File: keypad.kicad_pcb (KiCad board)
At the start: 2 copper layers, 67 x 105 mm, 10 parts, among them SW1 SW_Push, SW2 SW_Push, SW3 SW_Push, SW4 SW_Push, SW5 SW_Push, SW6 SW_Push, SW7 SW_Push, SW8 SW_Push, SW9 SW_Push, U1 ESP32-S3-DevKitC-1

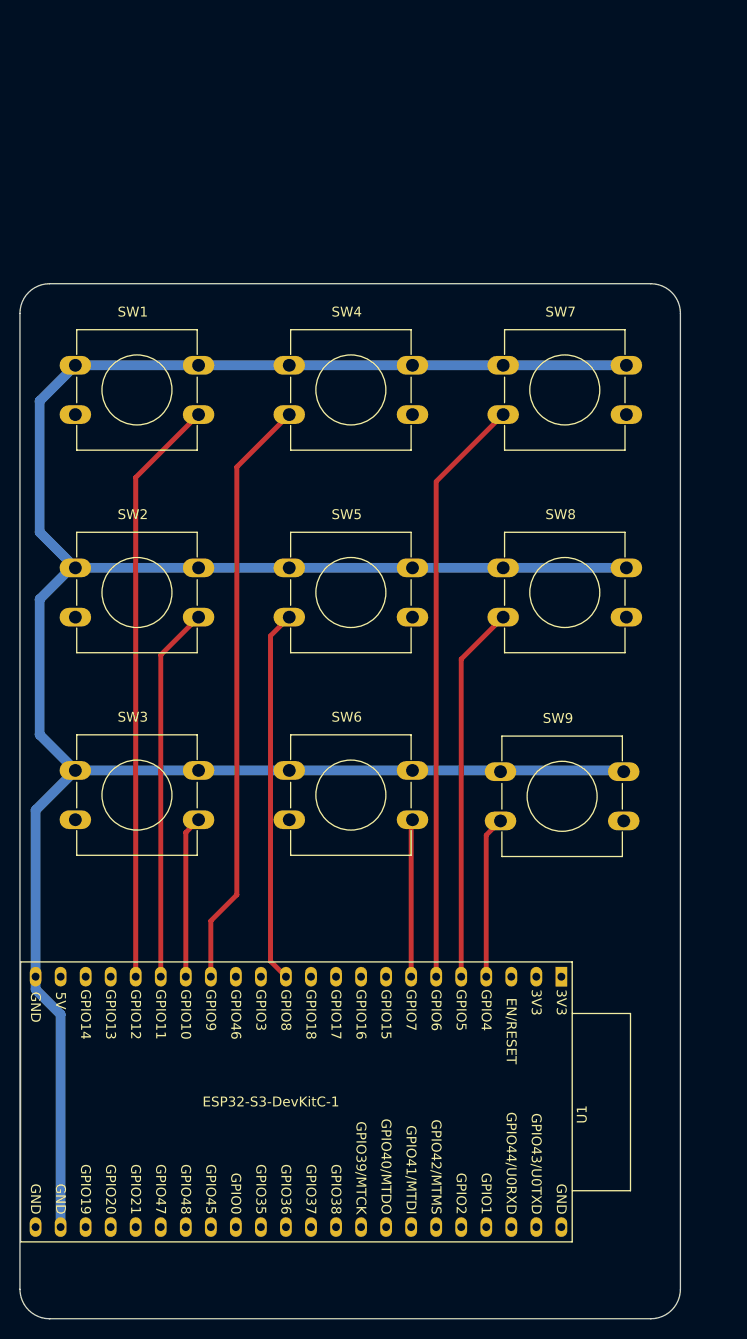
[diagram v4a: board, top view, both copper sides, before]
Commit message: add mounting holes
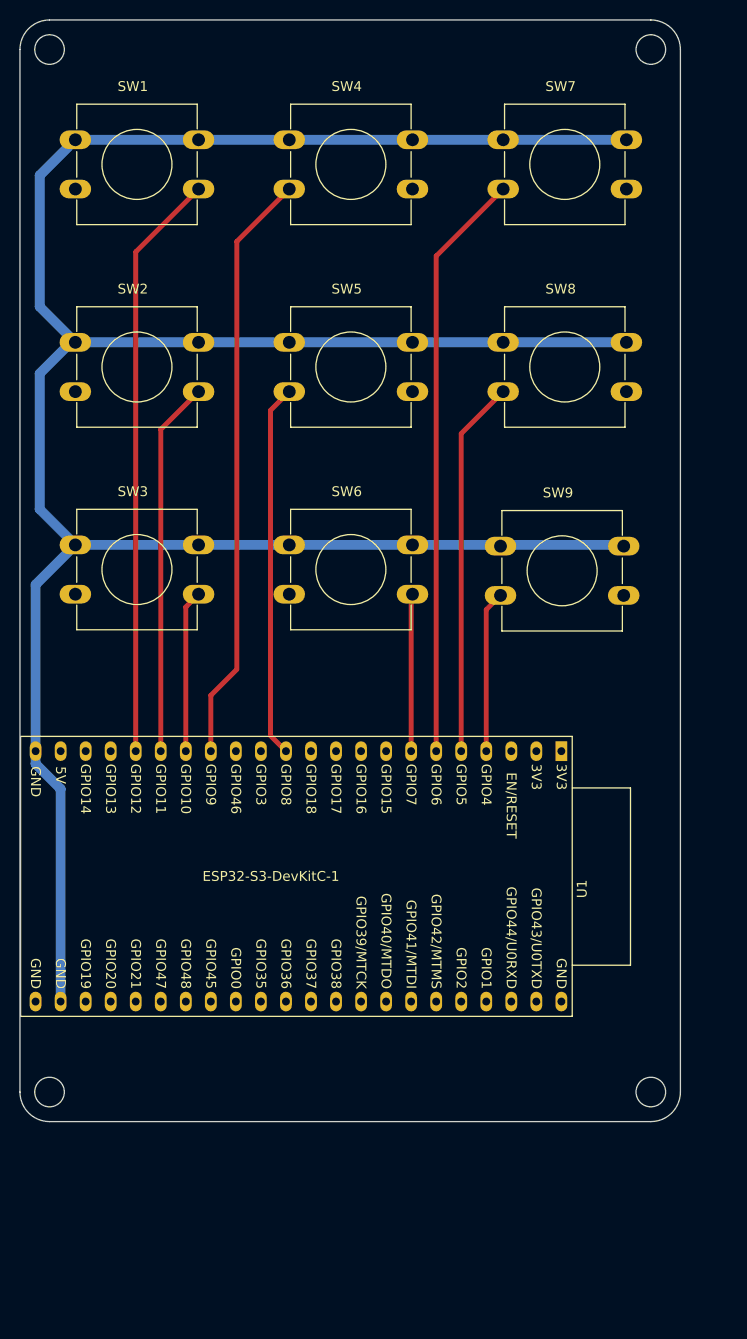
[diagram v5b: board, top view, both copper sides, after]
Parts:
- moved U1 22.9 mm to (172.9, 105.4)
- moved SW1 22.9 mm to (123.6, 43.4)
- moved SW2 22.9 mm to (123.6, 63.9)
- moved SW3 22.9 mm to (123.6, 84.5)
- moved SW4 22.9 mm to (145.3, 43.4)
- moved SW5 22.9 mm to (145.3, 63.9)
- moved SW6 22.9 mm to (145.3, 84.5)
- moved SW7 22.9 mm to (167.0, 43.4)
- moved SW8 22.9 mm to (167.0, 63.9)
- moved SW9 22.9 mm to (166.8, 84.6)
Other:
- board size 67 x 105 mm -> 67 x 111.8 mm

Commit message: add some art
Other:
- board text added: "gavhu10/keypad"
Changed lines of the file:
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@@
 		(capping no)
 		(filling no)
-		(zone_defaults)
 		(pcbplotparams
 			(layerselection 0x00000000_00000000_55555555_5755f5ff)
@@
 	)
 	(gr_line
+		(start 127.015013 96.441276)
+		(end 141.267947 75.971619)
+		(stroke
+			(width 0.839314)
+			(type default)
+		)
+		(layer "B.SilkS")
+	)
+	(gr_line
+		(start 131.082014 96.434741)
+		(end 127.015013 96.441276)
+		(stroke
+			(width 0.839314)
+			(type default)
+		)
+		(layer "B.SilkS")
+	)
+	(gr_line
+		(start 141.267947 75.971619)
+		(end 143.379781 78.326509)
+		(stroke
+			(width 0.839314)
+			(type default)
+		)
+		(layer "B.SilkS")
+	)
+	(gr_line
+		(start 143.379781 78.326509)
+		(end 131.082014 96.434741)
+		(stroke
+			(width 0.839314)
+			(type default)
+		)
+		(layer "B.SilkS")
+	)
+	(gr_line
+		(start 149.633081 85.269967)
+		(end 129.341772 62.68312)
+		(stroke
+			(width 0.839314)
+			(type default)
+		)
+		(layer "B.SilkS")
+	)
+	(gr_line
+		(start 149.636118 62.786378)
+		(end 149.636118 96.531626)
+		(stroke
+			(width 0.839314)
+			(type default)
+		)
+		(layer "B.SilkS")
+	)
+	(gr_line
+		(start 151.57 62.786378)
+		(end 149.636118 62.786378)
+		(stroke
+			(width 0.839314)
+			(type default)
+		)
+		(layer "B.SilkS")
+	)
+	(gr_line
+		(start 151.57 80.88632)
+		(end 151.57 62.786378)
+		(stroke
+			(width 0.839314)
+			(type default)
+		)
+		(layer "B.SilkS")
+	)
+	(gr_line
+		(start 152.614606 46.711926)
+		(end 177.160155 46.711926)
+		(stroke
+			(width 0.839314)
+			(type default)
+		)
+		(layer "B.SilkS")
+	)
+	(gr_line
+		(start 177.160155 46.711926)
+		(end 177.160155 80.88632)
+		(stroke
+			(width 0.839314)
+			(type default)
+		)
+		(layer "B.SilkS")
+	)
+	(gr_line
+		(start 177.160155 80.88632)
+		(end 151.57 80.88632)
+		(stroke
+			(width 0.839314)
+			(type default)
+		)
+		(layer "B.SilkS")
+	)
+	(gr_line
 		(start 118 34.24264)
 		(end 118 140)
@@
 		(layer "Edge.Cuts")
 	)
-	(segment
-		(start 140 53.71632)
-		(end 140 97.12132)
-		(width 0.5)
-		(layer "F.Cu")
-		(net "Net-(U1-GPIO9{slash}ADC1_CH8)")
-	)
-	(segment
-		(start 145.32 48.39632)
-		(end 140 53.71632)
-		(width 0.5)
-		(layer "F.Cu")
-		(net "Net-(U1-GPIO9{slash}ADC1_CH8)")
-	)
-	(segment
-		(start 137.36344 99.75788)
-		(end 137.36344 105.42132)
-		(width 0.5)
-		(layer "F.Cu")
-		(net "Net-(U1-GPIO9{slash}ADC1_CH8)")
-	)
-	(segment
-		(start 140 97.12132)
-		(end 137.36344 99.75788)
-		(width 0.5)
-		(layer "F.Cu")
-		(net "Net-(U1-GPIO9{slash}ADC1_CH8)")
+	(gr_text "gavhu10/keypad"
+		(at 132 138 0)
+		(layer "F.SilkS")
+		(effects
+			(font
+				(size 2 2)
+				(thickness 0.1)
+			)
+			(justify left bottom)
+		)
 	)
 	(segment
@@
 	)
 	(segment
-		(start 134.82344 105.42132)
-		(end 134.82344 90.79288)
+		(start 157.68344 89.63288)
+		(end 157.82 89.49632)
 		(width 0.5)
 		(layer "F.Cu")
-		(net "Net-(U1-GPIO10{slash}ADC1_CH9)")
+		(net "Net-(U1-GPIO7{slash}ADC1_CH6)")
 	)
 	(segment
-		(start 134.82344 90.79288)
-		(end 136.12 89.49632)
+		(start 157.68344 105.42132)
+		(end 157.68344 89.63288)
 		(width 0.5)
 		(layer "F.Cu")
-		(net "Net-(U1-GPIO10{slash}ADC1_CH9)")
+		(net "Net-(U1-GPIO7{slash}ADC1_CH6)")
 	)
 	(segment
-		(start 162.76344 105.42132)
-		(end 162.76344 73.20288)
+		(start 160.22344 105.42132)
+		(end 160.22344 55.19288)
 		(width 0.5)
 		(layer "F.Cu")
-		(net "Net-(U1-GPIO5{slash}ADC1_CH4)")
+		(net "Net-(U1-GPIO6{slash}ADC1_CH5)")
 	)
 	(segment
-		(start 162.76344 73.20288)
-		(end 167.02 68.94632)
+		(start 160.22344 55.19288)
+		(end 167.02 48.39632)
 		(width 0.5)
 		(layer "F.Cu")
-		(net "Net-(U1-GPIO5{slash}ADC1_CH4)")
+		(net "Net-(U1-GPIO6{slash}ADC1_CH5)")
+	)
+	(segment
+		(start 132.28344 105.42132)
+		(end 132.28344 72.78288)
+		(width 0.5)
+		(layer "F.Cu")
+		(net "Net-(U1-GPIO11{slash}ADC2_CH0)")
+	)
+	(segment
+		(start 132.28344 72.78288)
+		(end 136.12 68.94632)
+		(width 0.5)
+		(layer "F.Cu")
+		(net "Net-(U1-GPIO11{slash}ADC2_CH0)")
 	)
 	(segment
@@
 	)
 	(segment
-		(start 160.22344 105.42132)
-		(end 160.22344 55.19288)
+		(start 162.76344 105.42132)
+		(end 162.76344 73.20288)
 		(width 0.5)
 		(layer "F.Cu")
-		(net "Net-(U1-GPIO6{slash}ADC1_CH5)")
+		(net "Net-(U1-GPIO5{slash}ADC1_CH4)")
 	)
 	(segment
-		(start 160.22344 55.19288)
-		(end 167.02 48.39632)
+		(start 162.76344 73.20288)
+		(end 167.02 68.94632)
 		(width 0.5)
 		(layer "F.Cu")
-		(net "Net-(U1-GPIO6{slash}ADC1_CH5)")
+		(net "Net-(U1-GPIO5{slash}ADC1_CH4)")
 	)
 	(segment
-		(start 157.68344 89.63288)
-		(end 157.82 89.49632)
+		(start 140 53.71632)
+		(end 140 97.12132)
 		(width 0.5)
 		(layer "F.Cu")
-		(net "Net-(U1-GPIO7{slash}ADC1_CH6)")
+		(net "Net-(U1-GPIO9{slash}ADC1_CH8)")
 	)
 	(segment
-		(start 157.68344 105.42132)
-		(end 157.68344 89.63288)
+		(start 145.32 48.39632)
+		(end 140 53.71632)
 		(width 0.5)
 		(layer "F.Cu")
-		(net "Net-(U1-GPIO7{slash}ADC1_CH6)")
+		(net "Net-(U1-GPIO9{slash}ADC1_CH8)")
 	)
 	(segment
-		(start 132.28344 105.42132)
-		(end 132.28344 72.78288)
+		(start 137.36344 99.75788)
+		(end 137.36344 105.42132)
 		(width 0.5)
 		(layer "F.Cu")
-		(net "Net-(U1-GPIO11{slash}ADC2_CH0)")
+		(net "Net-(U1-GPIO9{slash}ADC1_CH8)")
 	)
 	(segment
-		(start 132.28344 72.78288)
-		(end 136.12 68.94632)
+		(start 140 97.12132)
+		(end 137.36344 99.75788)
 		(width 0.5)
 		(layer "F.Cu")
-		(net "Net-(U1-GPIO11{slash}ADC2_CH0)")
+		(net "Net-(U1-GPIO9{slash}ADC1_CH8)")
+	)
+	(segment
+		(start 134.82344 105.42132)
+		(end 134.82344 90.79288)
+		(width 0.5)
+		(layer "F.Cu")
+		(net "Net-(U1-GPIO10{slash}ADC1_CH9)")
+	)
+	(segment
+		(start 134.82344 90.79288)
+		(end 136.12 89.49632)
+		(width 0.5)
+		(layer "F.Cu")
+		(net "Net-(U1-GPIO10{slash}ADC1_CH9)")
 	)
 	(segment
@@
 		(net "Net-(U1-GPIO12{slash}ADC2_CH1)")
 	)
+	(group ""
+		(members "055c3a93-2d91-4d94-a0e1-0d276c22b7af" "1a785c4f-a8ad-4acc-b072-258b6932d9d1"
+			"4beef5e2-7c6e-4bf5-981f-f7f2c97805b4" "5a9348e2-e8fe-4e27-9830-7a686205907f"
+			"5bd682f7-9f95-4c47-b35e-df0fc1c0cef0" "88bb53e2-a4b4-4a37-b50f-d86c4b7a6131"
+			"af3630da-6659-4fc4-a180-c911d6de5f41" "b9c8238f-2934-4740-88ab-6a24f9f6ff63"
+			"cad80886-e45d-479f-9af1-23b4fd7b7647" "e8d27f2e-1b60-4680-8e6d-b658384dd067"
+			"ee033cae-9df1-4d2a-bbd3-eb6de77484f3"
+		)
+	)
 	(embedded_fonts no)

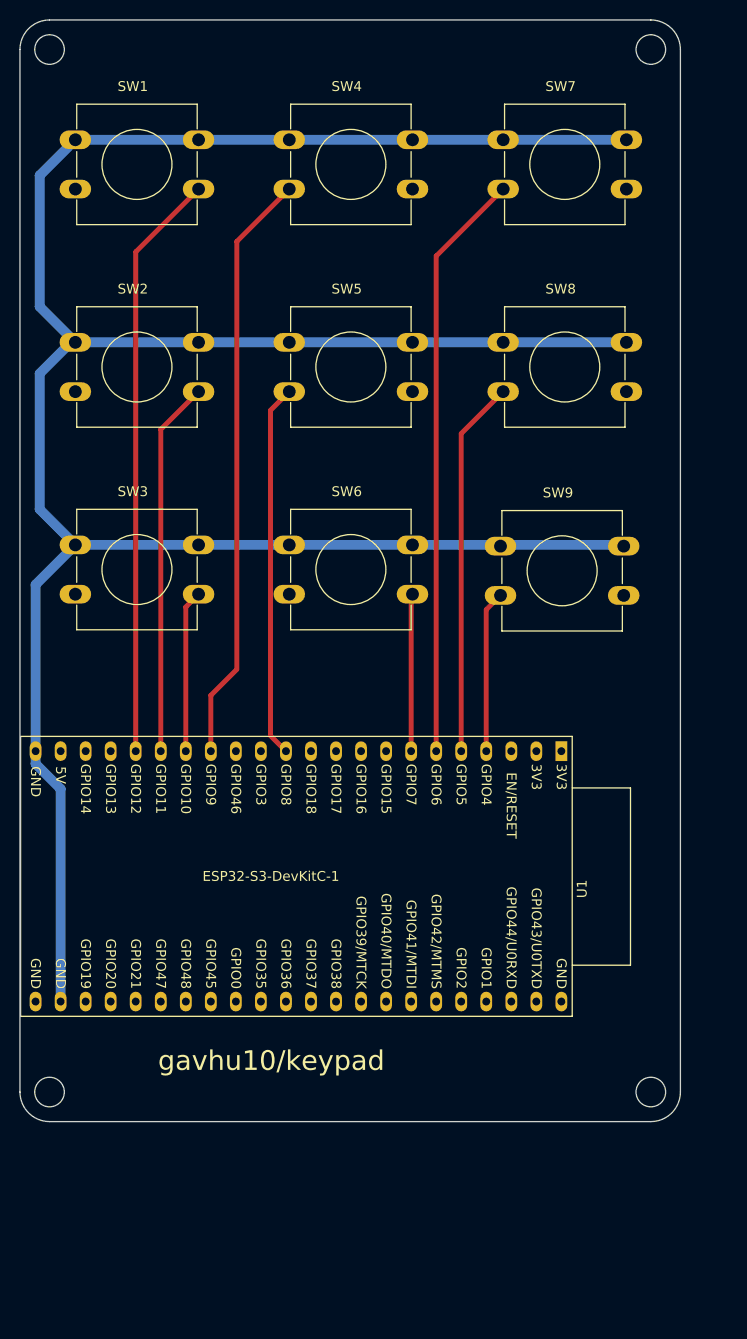
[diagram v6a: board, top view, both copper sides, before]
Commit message: fix drc errors and violations
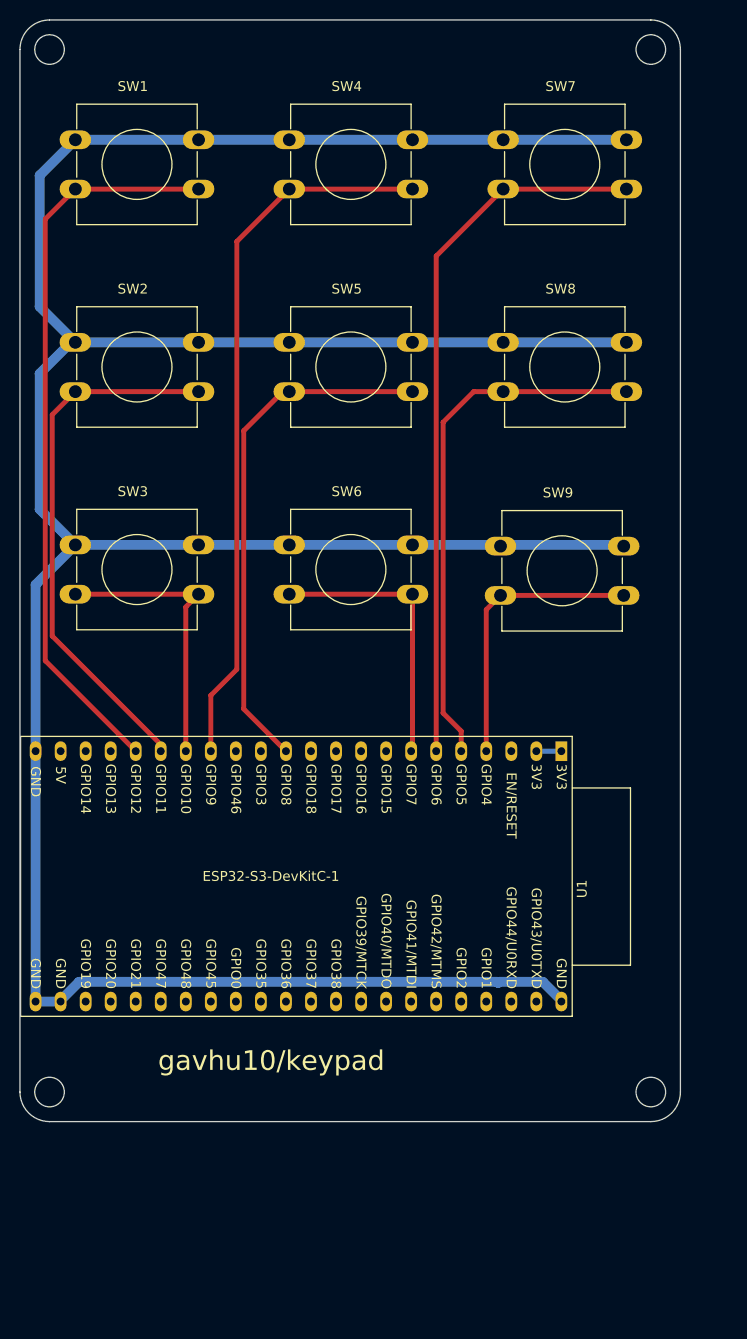
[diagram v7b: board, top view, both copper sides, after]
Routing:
- net GND: track 263.9 -> 318.1 mm
- net Net-(U1-GPIO11/ADC2_CH0): track 38.1 -> 54.5 mm
- net Net-(U1-GPIO5/ADC1_CH4): track 38.2 -> 54.0 mm
- net Net-(U1-GPIO8/ADC1_CH7): track 37.9 -> 53.0 mm
- net Net-(U1-GPIO12/ADC2_CH1): track 59.7 -> 74.6 mm
- net Net-(U1-GPIO7/ADC1_CH6): track 16.0 -> 28.7 mm
- net Net-(U1-GPIO9/ADC1_CH8): track 60.3 -> 72.8 mm
- net Net-(U1-GPIO6/ADC1_CH5): track 59.8 -> 72.3 mm
- net Net-(U1-GPIO4/ADC1_CH3): track 16.4 -> 28.9 mm
- net Net-(U1-GPIO10/ADC1_CH9): track 16.5 -> 29.0 mm
- net Net-(U1-3V3-Pad1): track 0.00 -> 2.54 mm

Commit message: reroute board
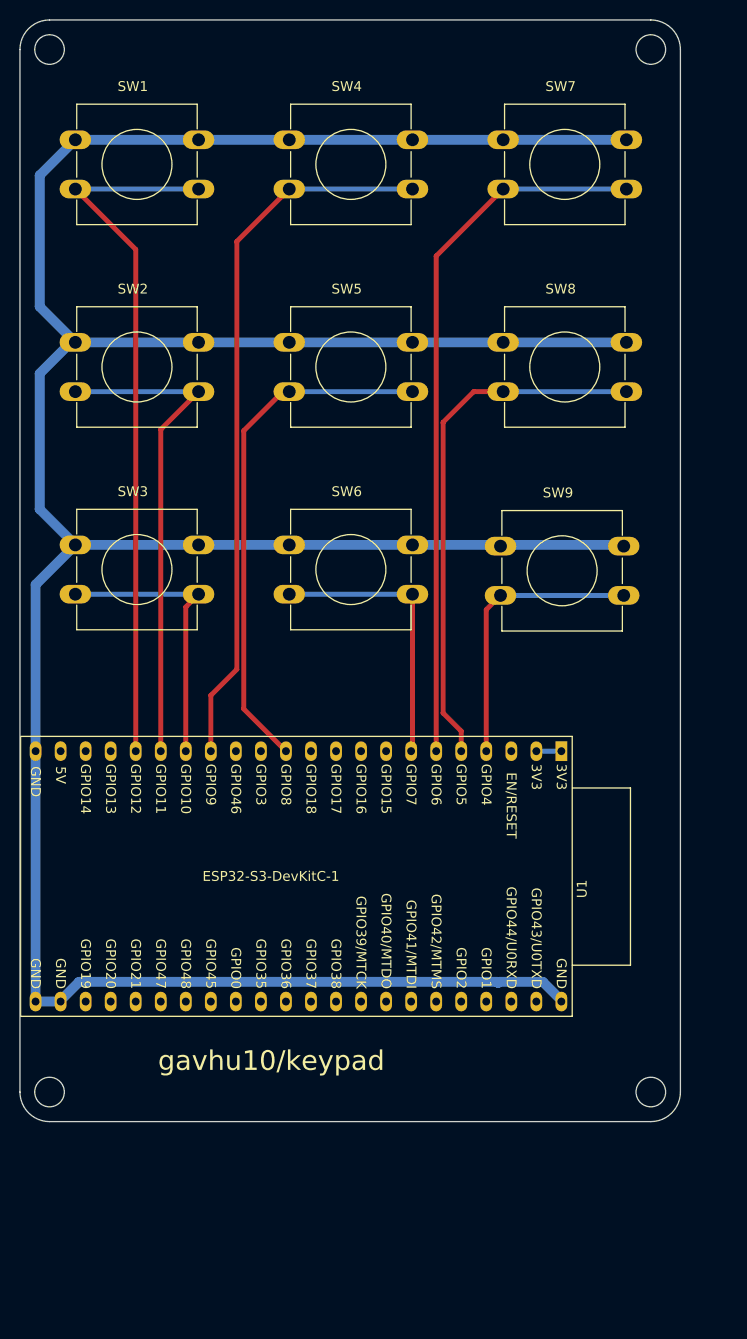
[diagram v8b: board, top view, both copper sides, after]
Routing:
- net Net-(U1-GPIO11/ADC2_CH0): track 54.5 -> 50.6 mm
- net Net-(U1-GPIO12/ADC2_CH1): track 74.6 -> 72.1 mm
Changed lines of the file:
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@@
 		(end 157.82 89.49632)
 		(width 0.5)
-		(layer "F.Cu")
+		(layer "B.Cu")
 		(net "Net-(U1-GPIO7{slash}ADC1_CH6)")
 	)
@@
 		(end 179.52 48.39632)
 		(width 0.5)
-		(layer "F.Cu")
+		(layer "B.Cu")
 		(net "Net-(U1-GPIO6{slash}ADC1_CH5)")
 	)
 	(segment
-		(start 123.62 68.94632)
-		(end 121.27 71.29632)
+		(start 132.28344 72.78288)
+		(end 132.28344 105.42132)
 		(width 0.5)
 		(layer "F.Cu")
@@
 	)
 	(segment
-		(start 132.28344 104.753491)
-		(end 132.28344 105.42132)
-		(width 0.5)
-		(layer "F.Cu")
-		(net "Net-(U1-GPIO11{slash}ADC2_CH0)")
-	)
-	(segment
-		(start 121.27 93.740051)
-		(end 132.28344 104.753491)
+		(start 136.12 68.94632)
+		(end 132.28344 72.78288)
 		(width 0.5)
 		(layer "F.Cu")
@@
 		(end 136.12 68.94632)
 		(width 0.5)
-		(layer "F.Cu")
-		(net "Net-(U1-GPIO11{slash}ADC2_CH0)")
-	)
-	(segment
-		(start 121.27 71.29632)
-		(end 121.27 93.740051)
-		(width 0.5)
-		(layer "F.Cu")
+		(layer "B.Cu")
 		(net "Net-(U1-GPIO11{slash}ADC2_CH0)")
 	)
@@
 	)
 	(segment
+		(start 140.7 101.13788)
+		(end 144.98344 105.42132)
+		(width 0.5)
+		(layer "F.Cu")
+		(net "Net-(U1-GPIO8{slash}ADC1_CH7)")
+	)
+	(segment
+		(start 145.32 68.94632)
+		(end 144.67 68.94632)
+		(width 0.5)
+		(layer "F.Cu")
+		(net "Net-(U1-GPIO8{slash}ADC1_CH7)")
+	)
+	(segment
 		(start 145.32 68.94632)
 		(end 157.82 68.94632)
 		(width 0.5)
-		(layer "F.Cu")
-		(net "Net-(U1-GPIO8{slash}ADC1_CH7)")
-	)
-	(segment
-		(start 140.7 101.13788)
-		(end 144.98344 105.42132)
-		(width 0.5)
-		(layer "F.Cu")
-		(net "Net-(U1-GPIO8{slash}ADC1_CH7)")
-	)
-	(segment
-		(start 145.32 68.94632)
-		(end 144.67 68.94632)
-		(width 0.5)
-		(layer "F.Cu")
+		(layer "B.Cu")
 		(net "Net-(U1-GPIO8{slash}ADC1_CH7)")
 	)
@@
 	)
 	(segment
+		(start 165.30344 91.06788)
+		(end 166.75 89.62132)
+		(width 0.5)
+		(layer "F.Cu")
+		(net "Net-(U1-GPIO4{slash}ADC1_CH3)")
+	)
+	(segment
+		(start 165.30344 105.42132)
+		(end 165.30344 91.06788)
+		(width 0.5)
+		(layer "F.Cu")
+		(net "Net-(U1-GPIO4{slash}ADC1_CH3)")
+	)
+	(segment
 		(start 166.75 89.62132)
 		(end 179.25 89.62132)
 		(width 0.5)
-		(layer "F.Cu")
-		(net "Net-(U1-GPIO4{slash}ADC1_CH3)")
-	)
-	(segment
-		(start 165.30344 91.06788)
-		(end 166.75 89.62132)
-		(width 0.5)
-		(layer "F.Cu")
-		(net "Net-(U1-GPIO4{slash}ADC1_CH3)")
-	)
-	(segment
-		(start 165.30344 105.42132)
-		(end 165.30344 91.06788)
-		(width 0.5)
-		(layer "F.Cu")
+		(layer "B.Cu")
 		(net "Net-(U1-GPIO4{slash}ADC1_CH3)")
 	)
@@
 	(segment
 		(start 167.02 68.94632)
-		(end 179.52 68.94632)
-		(width 0.5)
-		(layer "F.Cu")
-		(net "Net-(U1-GPIO5{slash}ADC1_CH4)")
-	)
-	(segment
-		(start 167.02 68.94632)
 		(end 164.03712 68.94632)
 		(width 0.5)
@@
 	)
 	(segment
+		(start 167.02 68.94632)
+		(end 179.52 68.94632)
+		(width 0.5)
+		(layer "B.Cu")
+		(net "Net-(U1-GPIO5{slash}ADC1_CH4)")
+	)
+	(segment
 		(start 140 53.71632)
 		(end 140 97.12132)
@@
 	)
 	(segment
+		(start 137.36344 99.75788)
+		(end 137.36344 105.42132)
+		(width 0.5)
+		(layer "F.Cu")
+		(net "Net-(U1-GPIO9{slash}ADC1_CH8)")
+	)
+	(segment
+		(start 140 97.12132)
+		(end 137.36344 99.75788)
+		(width 0.5)
+		(layer "F.Cu")
+		(net "Net-(U1-GPIO9{slash}ADC1_CH8)")
+	)
+	(segment
 		(start 145.32 48.39632)
 		(end 157.82 48.39632)
 		(width 0.5)
-		(layer "F.Cu")
-		(net "Net-(U1-GPIO9{slash}ADC1_CH8)")
-	)
-	(segment
-		(start 137.36344 99.75788)
-		(end 137.36344 105.42132)
-		(width 0.5)
-		(layer "F.Cu")
-		(net "Net-(U1-GPIO9{slash}ADC1_CH8)")
-	)
-	(segment
-		(start 140 97.12132)
-		(end 137.36344 99.75788)
-		(width 0.5)
-		(layer "F.Cu")
-		(net "Net-(U1-GPIO9{slash}ADC1_CH8)")
+		(layer "B.Cu")
+		(net "Net-(U1-GPIO9{slash}ADC1_CH8)")
+	)
+	(segment
+		(start 134.82344 105.42132)
+		(end 134.82344 90.79288)
+		(width 0.5)
+		(layer "F.Cu")
+		(net "Net-(U1-GPIO10{slash}ADC1_CH9)")
+	)
+	(segment
+		(start 134.82344 90.79288)
+		(end 136.12 89.49632)
+		(width 0.5)
+		(layer "F.Cu")
+		(net "Net-(U1-GPIO10{slash}ADC1_CH9)")
 	)
 	(segment
@@
 		(end 136.12 89.49632)
 		(width 0.5)
-		(layer "F.Cu")
+		(layer "B.Cu")
 		(net "Net-(U1-GPIO10{slash}ADC1_CH9)")
 	)
 	(segment
-		(start 134.82344 105.42132)
-		(end 134.82344 90.79288)
-		(width 0.5)
-		(layer "F.Cu")
-		(net "Net-(U1-GPIO10{slash}ADC1_CH9)")
-	)
-	(segment
-		(start 134.82344 90.79288)
-		(end 136.12 89.49632)
-		(width 0.5)
-		(layer "F.Cu")
-		(net "Net-(U1-GPIO10{slash}ADC1_CH9)")
+		(start 129.74344 54.51976)
+		(end 129.74344 105.42132)
+		(width 0.5)
+		(layer "F.Cu")
+		(net "Net-(U1-GPIO12{slash}ADC2_CH1)")
 	)
 	(segment
 		(start 123.62 48.39632)
-		(end 120.57 51.44632)
-		(width 0.5)
-		(layer "F.Cu")
-		(net "Net-(U1-GPIO12{slash}ADC2_CH1)")
-	)
-	(segment
-		(start 120.57 51.44632)
-		(end 120.57 96.24788)
-		(width 0.5)
-		(layer "F.Cu")
-		(net "Net-(U1-GPIO12{slash}ADC2_CH1)")
-	)
-	(segment
-		(start 120.57 96.24788)
-		(end 129.74344 105.42132)
+		(end 129.74344 54.51976)
 		(width 0.5)
 		(layer "F.Cu")
@@
 		(end 136.12 48.39632)
 		(width 0.5)
-		(layer "F.Cu")
+		(layer "B.Cu")
 		(net "Net-(U1-GPIO12{slash}ADC2_CH1)")
 	)
